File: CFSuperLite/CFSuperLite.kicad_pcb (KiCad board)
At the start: 2 copper layers, 99.9 x 99.9 mm, 23 parts, among them J1 IDE_CONNECTOR, J2 CF Adapter Power, J3 Bus_ISA_8bit, J4 Addresses, J5 Addresses, U1 BIOS FLASH, U2 74HCT245, U3 ATF/GAL22V10x-15, U4 DS1315, U5 AS6C4008-55PCN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

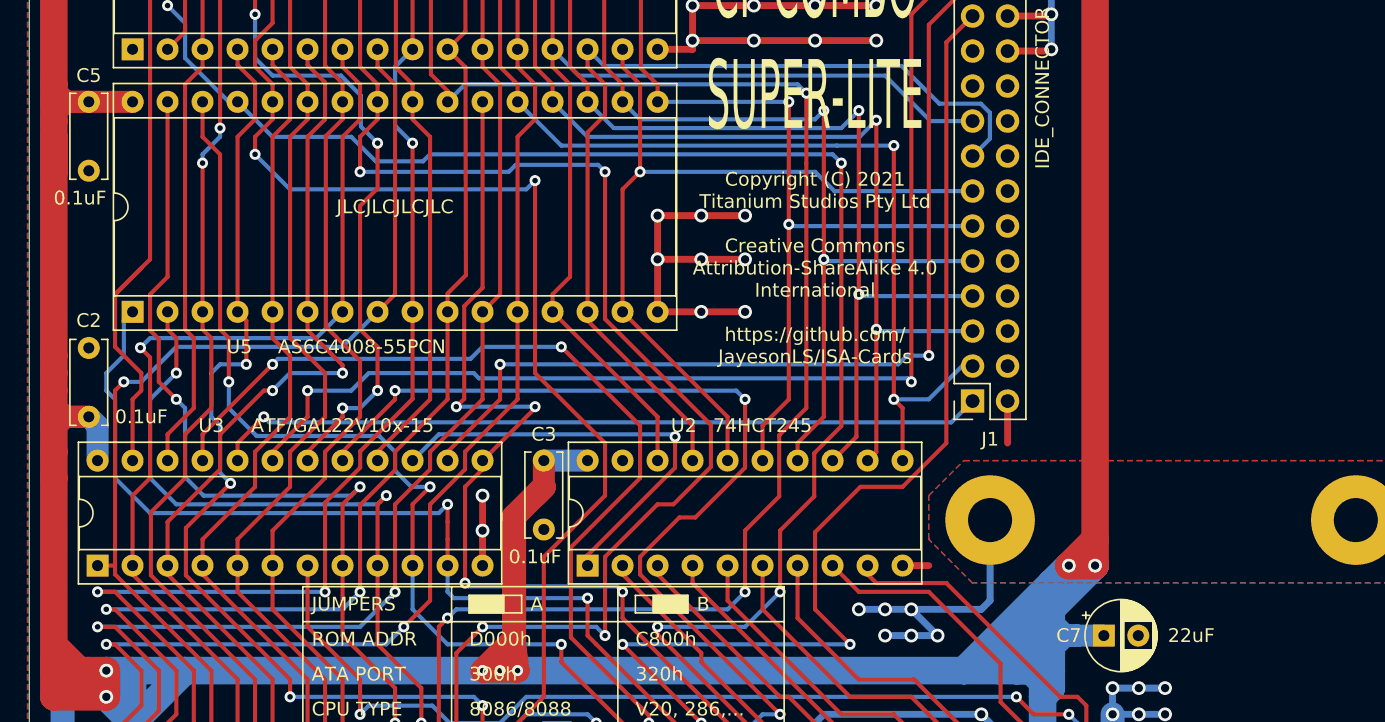
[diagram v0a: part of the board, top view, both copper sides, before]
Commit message: CFSuperLite: Mostly schematic work to direct-connect the SST flash to bus. Remove now-redundant signals from the glue and switch to a smaller 16V8 GAL. Layout needs to be redone. Should change some component selections first.
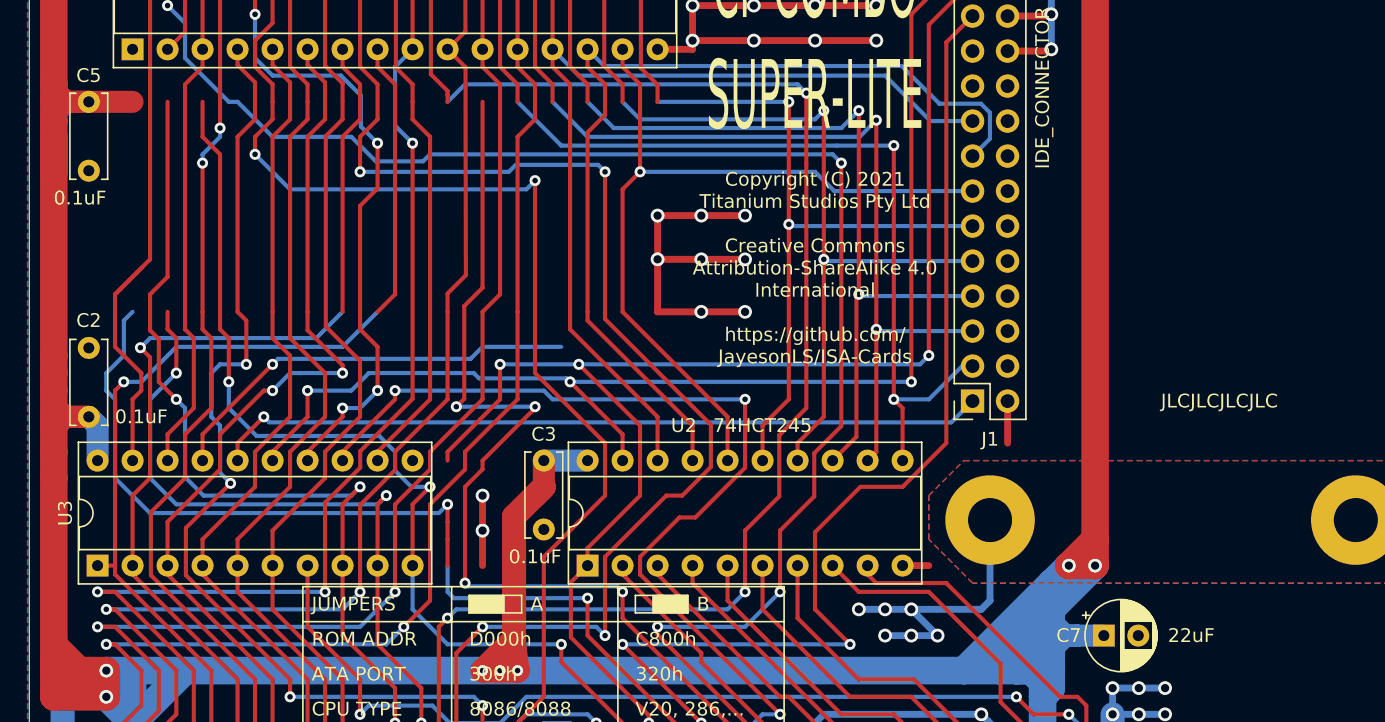
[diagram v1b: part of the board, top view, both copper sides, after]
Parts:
- removed U5: AS6C4008-55PCN, Package_DIP:DIP-32_W15.24mm_Socket
- U3: value ATF/GAL22V10x-15 -> ATF/GAL16V8x-15; footprint Package_DIP:DIP-24_W7.62mm_Socket -> Package_DIP:DIP-20_W7.62mm_Socket
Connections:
- J1 pad 25: ~IOR~_DELAYED -> ~IOR
- J3 pad 42: Net-(J3-Pad42) -> AEN
- U1 pad 13: D0_BUF -> D0
- U1 pad 14: D1_BUF -> D1
- U1 pad 15: D2_BUF -> D2
- U1 pad 17: D3_BUF -> D3
- U1 pad 18: D4_BUF -> D4
- U1 pad 19: D5_BUF -> D5
- U1 pad 20: D6_BUF -> D6
- U1 pad 21: D7_BUF -> D7
- U1 pad 24: ~MEMR~_DELAYED -> ~MEMR
- U2 pad 1: ~IOR_OR_MEMR -> ~IOR
- U2 pad 19: GND -> ~CS1~_ATA
- U3 pad 10: A17 -> GND
- U3 pad 11: A18 -> A17
- U3 pad 12: GND -> A18
- U3 pad 14: ~IOR~_DELAYED -> ~CE~_BIOS_DECODE
- U3 pad 15: ~IOR_OR_MEMR -> ~CS1~_ATA
- U3 pad 16: ~MEMR~_DELAYED -> ~RESET
- U3 pad 17: ~MEMR -> AEN
- U3 pad 18: ~CE~_BIOS_DECODE -> ATA_ADDR_JUMPER
- U3 pad 19: ~CS1~_ATA -> ROM_ADDR_JUMPER
- U3 pad 20: ~RESET -> VCC
- U4 pad 12: ~MEMR~_DELAYED -> ~MEMR
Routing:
- net ~IOR~_DELAYED: track 68.4 -> 0.00 mm, vias 2 -> 0
- net ~IOR: track 71.9 -> 108.0 mm, vias 3 -> 4
- net ~IOR_OR_MEMR: track 31.9 -> 0.00 mm, vias 1 -> 0
- net AEN: track 0.00 -> 30.6 mm, vias 0 -> 1
- net D4: track 27.3 -> 47.5 mm
- net D4_BUF: track 72.6 -> 52.4 mm
- net D7_BUF: track 78.6 -> 58.5 mm
- net D7: track 29.0 -> 49.1 mm
- net D5_BUF: track 75.6 -> 55.5 mm
- net D5: track 27.7 -> 47.8 mm
- net D6_BUF: track 77.2 -> 57.1 mm
- net D6: track 27.7 -> 47.8 mm
- net D3_BUF: track 69.8 -> 49.7 mm
- net D3: track 27.0 -> 47.0 mm
- net ~CS1~_ATA: track 96.9 -> 104.2 mm, vias 2 -> 3
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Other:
- board text removed: "Compact Flash with XT-IDE BIOS"
- board text removed: "Compact Flash with XT-IDE BIOS and SmartWatch"
- board text removed: "Compact Flash with XT-IDE BIOS, SmartWatch and 512K SRAM. For original Tandy 1000, 1000A or 1000 HD only. Remove any other RAM upgrade before installing."

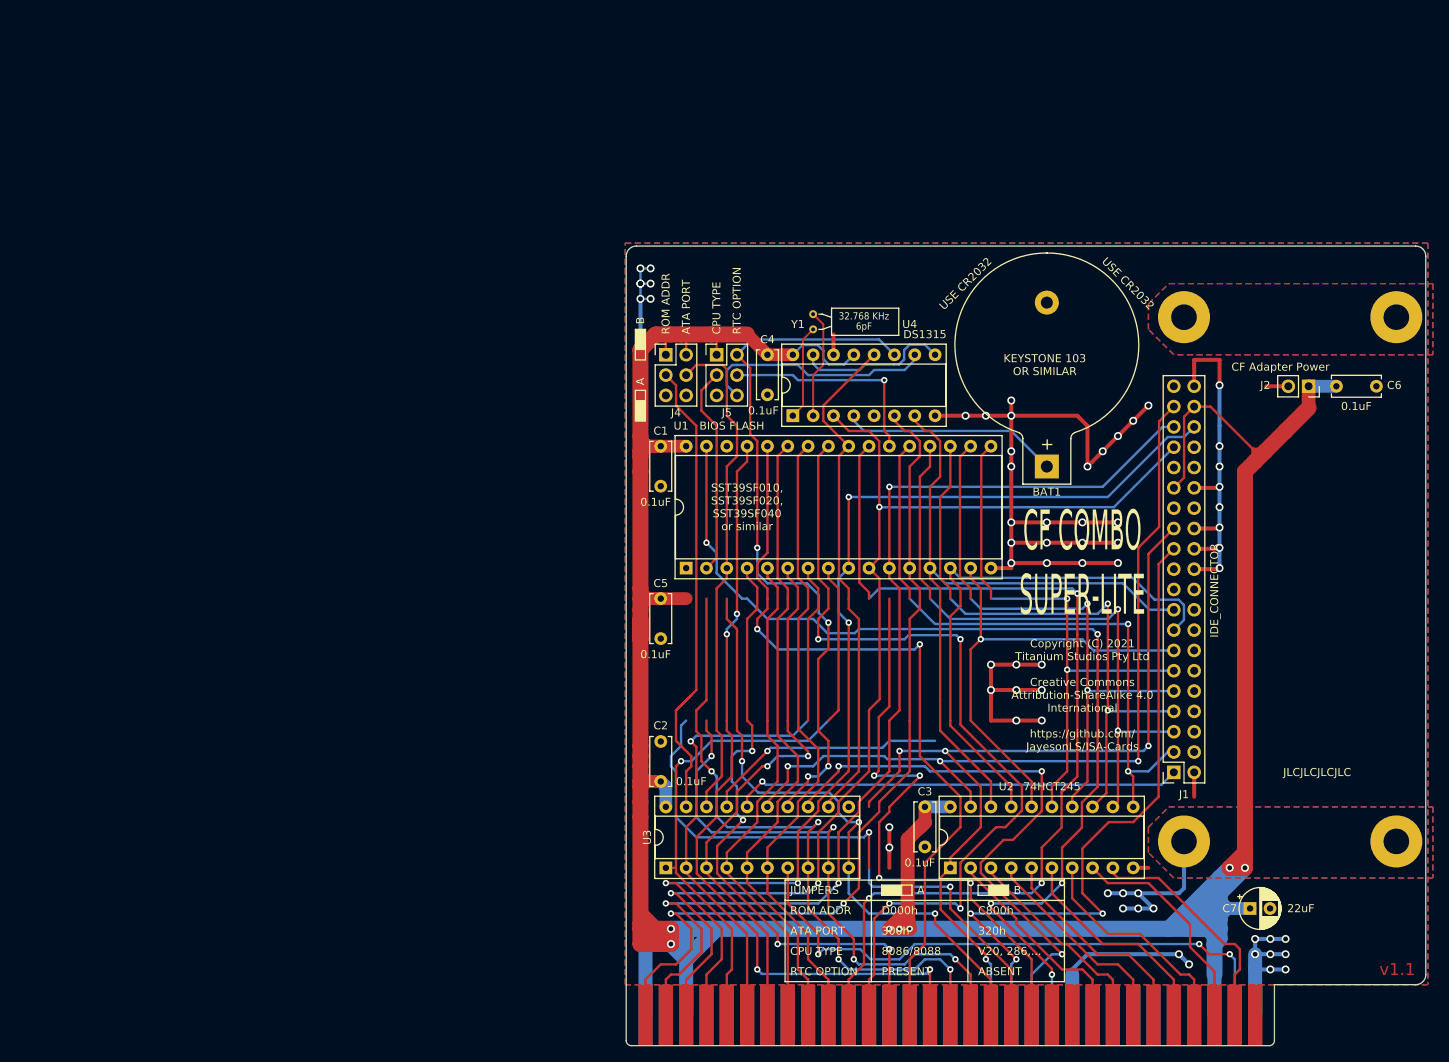
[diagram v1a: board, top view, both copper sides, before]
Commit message: WIP on CFSuperLite layout. Switched it to use a dip switch rather than jumpers.
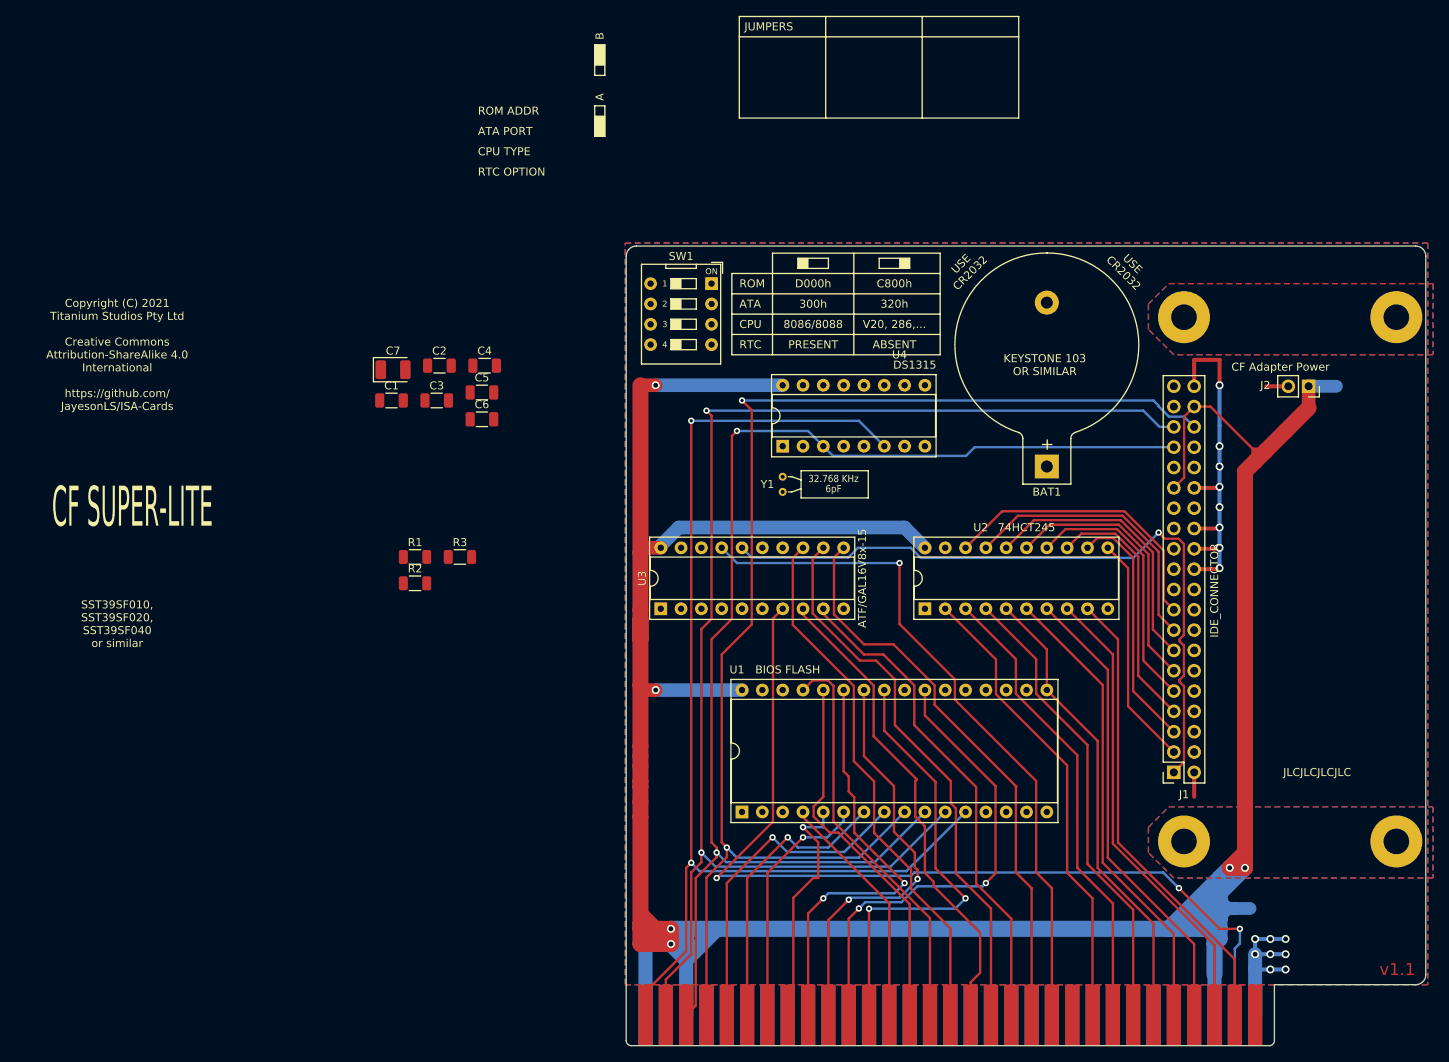
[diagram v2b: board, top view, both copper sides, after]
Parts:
- removed J4, J5: Addresses, Connector_PinHeader_2.54mm:PinHeader_2x03_P2.54mm_Vertical
- added R1: 10K, Resistor_SMD:R_1206_3216Metric, F.Cu at (70.3, 81.2)
- added R2: 10K, Resistor_SMD:R_1206_3216Metric, F.Cu at (70.3, 84.4)
- added R3: 10K, Resistor_SMD:R_1206_3216Metric, F.Cu at (75.9, 81.2)
- added SW1: Options, Button_Switch_THT:SW_DIP_SPSTx04_Slide_9.78x12.34mm_W7.62mm_P2.54mm, F.Cu at (107.3, 47.0)
- C1, C2, C3, C4, C5, C6: footprint Capacitor_THT:C_Disc_D6.0mm_W2.5mm_P5.00mm -> Capacitor_SMD:C_1206_3216Metric
- C7: value 22uF -> 22uF-33uF 16-25v; footprint Capacitor_THT:CP_Radial_D5.0mm_P2.50mm -> Capacitor_Tantalum_SMD:CP_EIA-3528-15_AVX-H
- moved C7 126.5 mm to (67.5, 57.7)
- moved C6 106.9 mm to (78.6, 63.9)
- moved C3 79.4 mm to (73.0, 61.6), turned to 0 degrees
- moved C2 58.9 mm to (73.3, 57.2), turned to 0 degrees
- moved C4 35.4 mm to (79.0, 57.2), turned to 0 degrees
- moved C1 34.1 mm to (67.3, 61.6), turned to 0 degrees
- moved C5 34.1 mm to (78.6, 60.6), turned to 0 degrees
- moved U2 32.5 mm to (134.0, 87.6)
- moved U3 32.4 mm to (101.0, 87.6)
- moved U1 31.3 mm to (111.1, 113.0)
- moved Y1 20.7 mm to (116.2, 73.0)
- moved U4 4.02 mm to (116.2, 67.3)
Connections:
- U1 pad 22: ~CE~_BIOS -> ~CE~_BIOS_THRU
- U3 pad 11: A17 -> A19
- U3 pad 12: A18 -> A17
- U3 pad 13: A19 -> A15
- U3 pad 8: A15 -> A16
- U3 pad 9: A16 -> A18
- U4 pad 10: ~CE~_BIOS_THRU -> Net-(U4-Pad10)
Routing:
- net GND: track 347.2 -> 146.1 mm, vias 64 -> 16
- net ~MEMW: track 127.6 -> 0.00 mm, vias 5 -> 0
- net ~IOR: track 108.0 -> 0.00 mm, vias 4 -> 0
- net ~CS1~_ATA: track 104.2 -> 0.00 mm, vias 3 -> 0
- net ~CE~_BIOS_DECODE: track 89.3 -> 0.00 mm, vias 4 -> 0
- net ~IOW: track 85.0 -> 0.00 mm, vias 3 -> 0
- net ~MEMR: track 73.2 -> 0.00 mm, vias 3 -> 0
- net A10: track 123.0 -> 59.3 mm, vias 3 -> 2
- net ~MEMR~_DELAYED: track 63.6 -> 0.00 mm
- net ATA_ADDR_JUMPER: track 63.2 -> 0.00 mm
- net ROM_ADDR_JUMPER: track 60.4 -> 0.00 mm
- net AEN: track 30.6 -> 87.4 mm
- net A11: track 108.8 -> 56.2 mm, vias 4 -> 2
- net D0_BUF: track 87.2 -> 36.6 mm
- net A13: track 97.2 -> 46.7 mm, vias 2 -> 0
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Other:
- board text added: "ATA"
- board text added: "CF SUPER-LITE"
- board text added: "CPU"
- board text added: "ROM"
- board text added: "RTC"
- board text removed: "CF COMBO SUPER-LITE"
- board text removed: "In memory of my father, Michael James Lee-Steere. Our early experiences with the Tandy 1000 provided the inspiration for creating this upgrade."

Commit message: CFSuperLite WIP.
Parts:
- removed the C5 at (78.6, 60.6)
- moved C6 135.6 mm to (185.2, 125.1)
- moved C5 108.2 mm to (186.7, 59.8)
- moved C2 63.4 mm to (134.0, 75.6), turned to 90 degrees
- moved C1 46.3 mm to (101.0, 93.3), turned to 90 degrees
- moved R2 36.6 mm to (102.2, 66.7)
- moved R1 33.9 mm to (102.2, 69.8)
- moved C4 32.9 mm to (111.8, 59.7), turned to 180 degrees
- moved R3 31.7 mm to (102.2, 63.5)
- moved C3 31.3 mm to (101.0, 75.6), turned to 90 degrees
- moved U1 10.2 mm to (101.0, 113.0)
- renumbered C6 to C5, C7 to C6
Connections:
- U3 pad 1: A04 -> A16
- U3 pad 13: A15 -> A05
- U3 pad 18: ATA_ADDR_JUMPER -> ROM_ADDR_JUMPER
- U3 pad 19: ROM_ADDR_JUMPER -> ATA_ADDR_JUMPER
- U3 pad 2: A05 -> A18
- U3 pad 3: A06 -> A15
- U3 pad 5: A08 -> A06
- U3 pad 6: A09 -> A08
- U3 pad 7: RESET -> A09
- U3 pad 8: A16 -> A04
- U3 pad 9: A18 -> RESET
- U4 pad 10: Net-(U4-Pad10) -> ~CE~_BIOS_THRU
- U4 pad 7: D0_BUF -> D0
- Y1 pad 1: /XTAL1 -> /XTAL2
- Y1 pad 2: /XTAL2 -> /XTAL1
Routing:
- net GND: track 146.1 -> 785.7 mm, vias 16 -> 32
- net ~MEMR: track 0.00 -> 114.9 mm, vias 0 -> 3
- net ~IOR: track 0.00 -> 109.0 mm, vias 0 -> 4
- net ~MEMW: track 0.00 -> 80.3 mm, vias 0 -> 2
- net ~CE~_BIOS_DECODE: track 0.00 -> 78.8 mm, vias 0 -> 2
- net ~CE~_BIOS_THRU: track 0.00 -> 78.7 mm, vias 0 -> 1
- net ~IOW: track 0.00 -> 74.1 mm, vias 0 -> 3
- net ATA_ADDR_JUMPER: track 0.00 -> 68.9 mm
- net ~CS1~_ATA: track 0.00 -> 68.8 mm, vias 0 -> 1
- net V20_JUMPER: track 0.00 -> 65.5 mm
- net RESET: track 116.7 -> 64.2 mm, vias 3 -> 2
- net D0: track 58.4 -> 102.0 mm, vias 0 -> 1
- net ROM_ADDR_JUMPER: track 0.00 -> 37.1 mm
- net A05: track 36.2 -> 67.5 mm
- net A06: track 31.1 -> 62.4 mm, vias 1 -> 3
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
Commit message: CFSuperLite: DRC passing and all pads connected. Needs clean up.
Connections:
- U3 pad 4: A07 -> A06
- U3 pad 5: A06 -> A07
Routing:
- net RESET: track 64.2 -> 102.6 mm, vias 2 -> 3
- net A07: track 27.8 -> 54.9 mm
- net A08: track 27.8 -> 54.3 mm
- net A02: track 157.4 -> 174.3 mm, vias 2 -> 4
- net VCC: track 437.2 -> 449.4 mm, vias 5 -> 6
- net GND: track 785.7 -> 779.9 mm
- net A03: track 152.8 -> 158.0 mm
- net A09: track 57.4 -> 54.3 mm
- net A11: track 46.6 -> 49.2 mm, vias 1 -> 2
- net A05: track 67.5 -> 65.5 mm
- net A06: track 62.4 -> 60.9 mm
- net ~CE~_BIOS_DECODE: track 78.8 -> 79.9 mm
- net A13: track 58.5 -> 59.6 mm
- net A14: track 60.2 -> 61.2 mm
- net A04: track 59.9 -> 58.8 mm, vias 1 -> 2
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
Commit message: CFSuperLite layout cleanup WIP.
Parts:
- moved C1 2.54 mm to (101.0, 95.9)
- moved U1 2.54 mm to (101.0, 115.6)
- moved Y1 0.64 mm to (116.2, 72.4)
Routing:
- net GND: track 779.9 -> 158.8 mm, vias 32 -> 35
- net A02: track 174.3 -> 167.8 mm
- net ~CE~_BIOS_THRU: track 78.7 -> 85.1 mm
- net A01: track 160.9 -> 157.2 mm
- net V20_JUMPER: track 65.5 -> 69.0 mm
- net A03: track 158.0 -> 154.8 mm
- net ~CE~_BIOS_DECODE: track 79.9 -> 76.8 mm
- net A00: track 130.9 -> 133.8 mm
- net VCC: track 449.4 -> 452.3 mm, vias 6 -> 8
- net ATA_ADDR_JUMPER: track 68.9 -> 71.6 mm
- net ~MEMW: track 80.3 -> 77.8 mm
- net A13: track 59.6 -> 57.1 mm
- net A10: track 44.0 -> 41.5 mm
- net A14: track 61.2 -> 58.7 mm
- net A11: track 49.2 -> 46.7 mm
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
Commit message: CFSuperLite layout cleanup more WIP.
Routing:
- net A04: track 58.8 -> 62.3 mm
- net A12: track 43.3 -> 45.8 mm
- net A05: track 65.5 -> 63.1 mm
- net RESET: track 105.0 -> 103.7 mm
- net D4_BUF: track 33.2 -> 34.4 mm
- net A01: track 157.2 -> 156.1 mm
- net D2: track 77.1 -> 76.0 mm
- net ~MEMW: track 77.8 -> 78.8 mm
- net D1: track 78.8 -> 77.8 mm
- net A00: track 133.8 -> 133.0 mm
- net A19: track 72.9 -> 72.2 mm
- net A13: track 57.1 -> 57.8 mm
- net A02: track 167.8 -> 167.1 mm
- net A18: track 86.6 -> 87.2 mm
- net D0: track 101.7 -> 101.2 mm
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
